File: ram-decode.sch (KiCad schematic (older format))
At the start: 13 parts, among them IC100 TBP24S10, IC102 74LS125, IC103 74LS74, IC52 74LS04, IC67 74LS20, IC70 74S00, IC8 74LS04, IC81 74LS08, IC85 74LS04, IC98 74LS138, IC99 74LS138, U102 74LS125

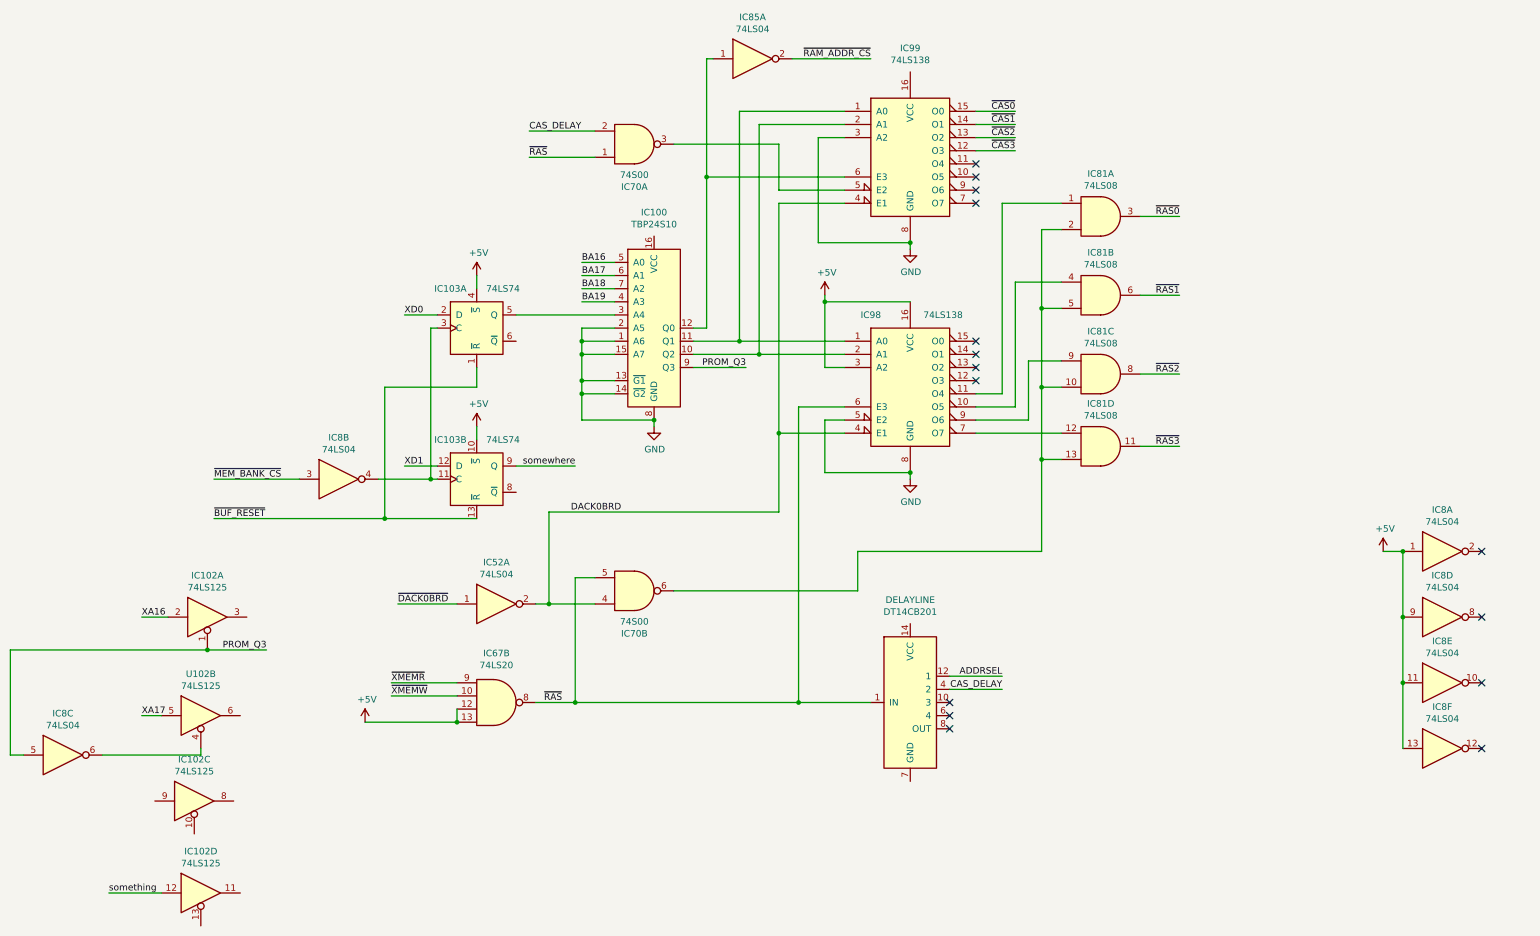
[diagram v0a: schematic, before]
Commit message: Tidy up and map all signals
This fixes up the schematic to:
 - Look presentable
 - Fix all labels connecting sheets
 - Tidy up all loose ends by either inspecting the PCB under
    magnification, measuring with an oscillosope or buzzing
    out with a meter
 - Pass ERC (with 1 exception due to incorrect circuitry around
    pin 33 on the FPU (~RQ~/~GT1~)
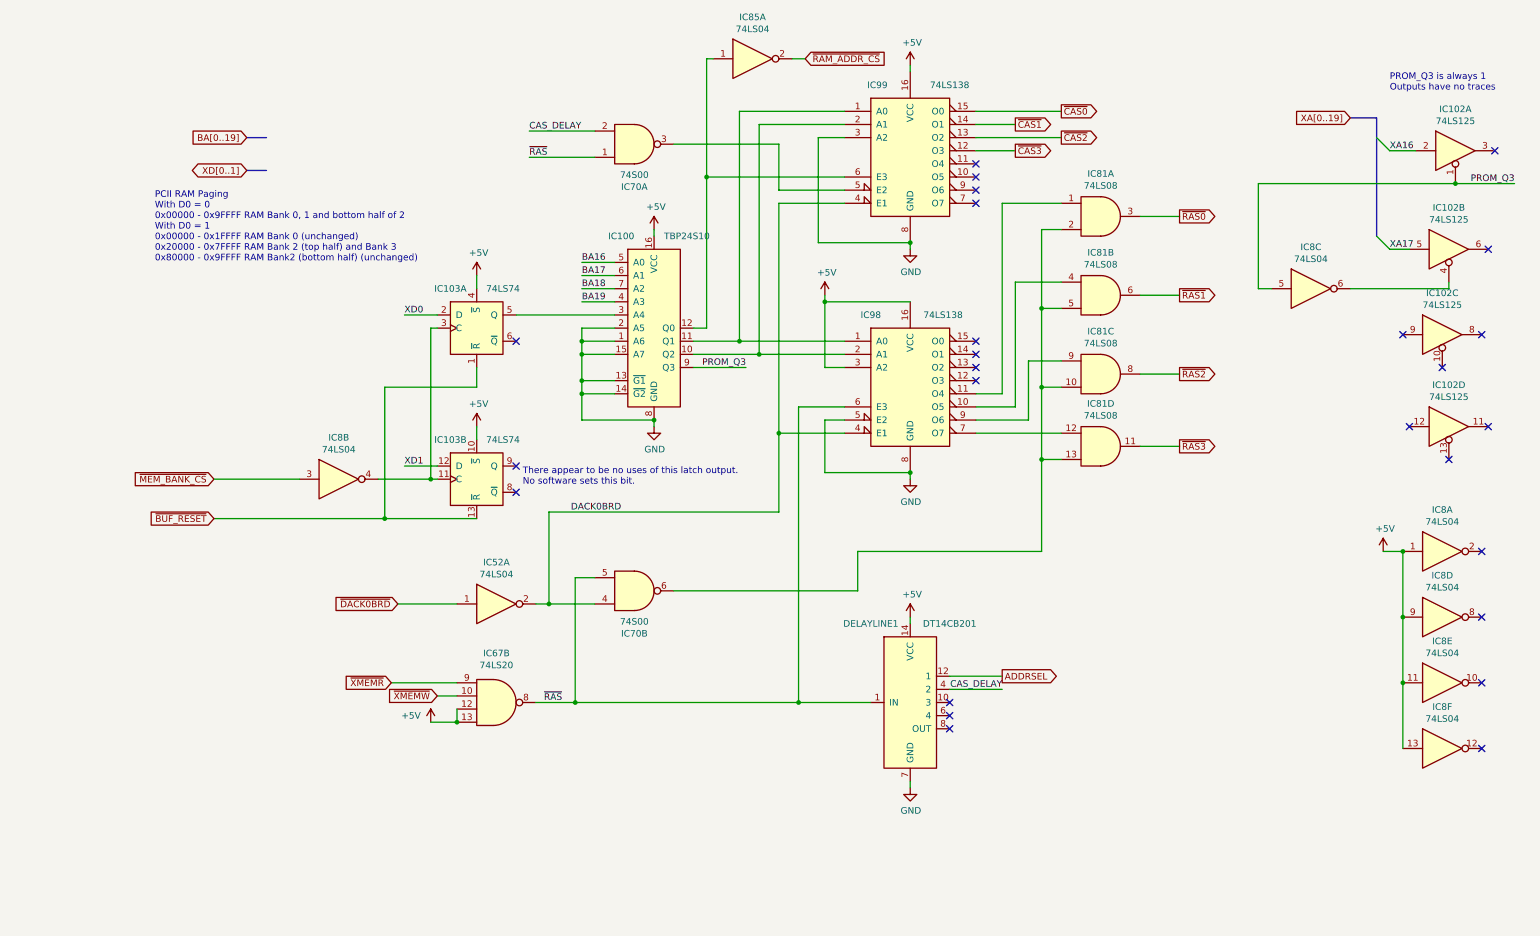
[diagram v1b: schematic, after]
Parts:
- renumbered DELAYLINE to DELAYLINE1, U102 to IC102
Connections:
- net +5V: now also DELAYLINE1.14 (VCC), IC100.16 (VCC), IC99.16 (VCC)
- net GND: now also DELAYLINE1.7 (GND)
- net something: no longer names the net of IC102.12
- net somewhere: no longer names the net of IC103.9 (Q)
- no-connect marks 15 -> 26
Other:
- note added: "PCII RAM Paging\nWith D0 = 0\n0x00000 - 0x9FFFF RAM Bank 0, 1 and bottom half of 2\nWith D0 = 1\n0x00000 - 0x1FFFF RAM Bank 0 (unchanged)\n0x20000 - 0x7FFFF RAM Bank 2 (top half) and Bank 3\n0x80000 - 0x9FFFF RAM Bank2 (bottom half) (unchanged)"
- note added: "PROM_Q3 is always 1\nOutputs have no traces"
- note added: "There appear to be no uses of this latch output.\nNo software sets this bit."
- moved on the sheet: IC102A, IC102B, IC102C, IC102D, IC8C
